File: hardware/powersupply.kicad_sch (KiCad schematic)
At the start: 34 parts, among them IC1 Battery_Charger, IC3 3.3V_Buck, J1 Battery, J1 Switch_In, J1 Switch_Out, J1 USB-C, Q2 PMV50XPAR, U2 5V_Boost

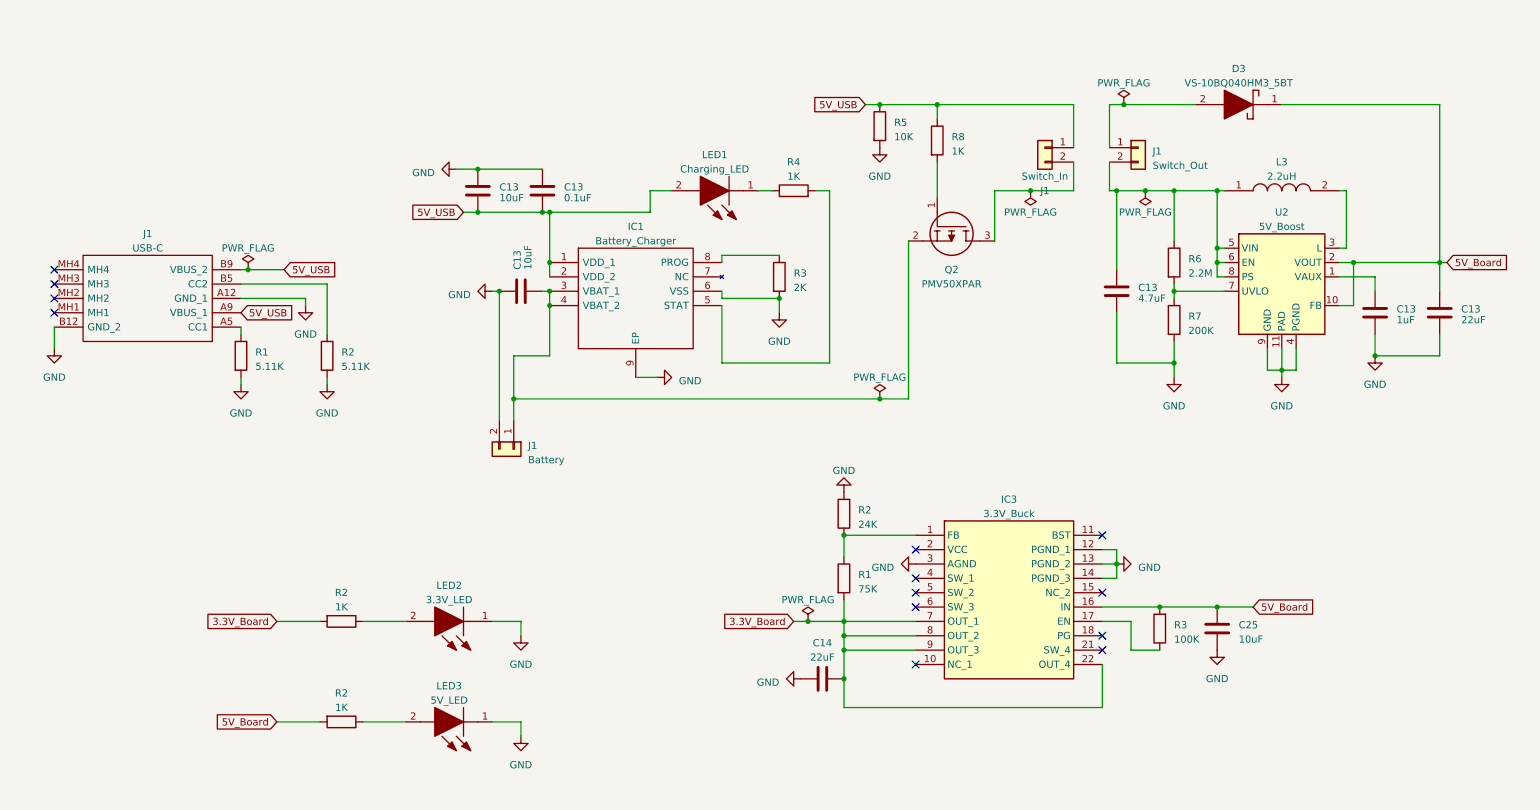
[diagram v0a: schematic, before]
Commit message: Change STM code to support an I2C bus. Add encoder reading code - tested on TIM1.
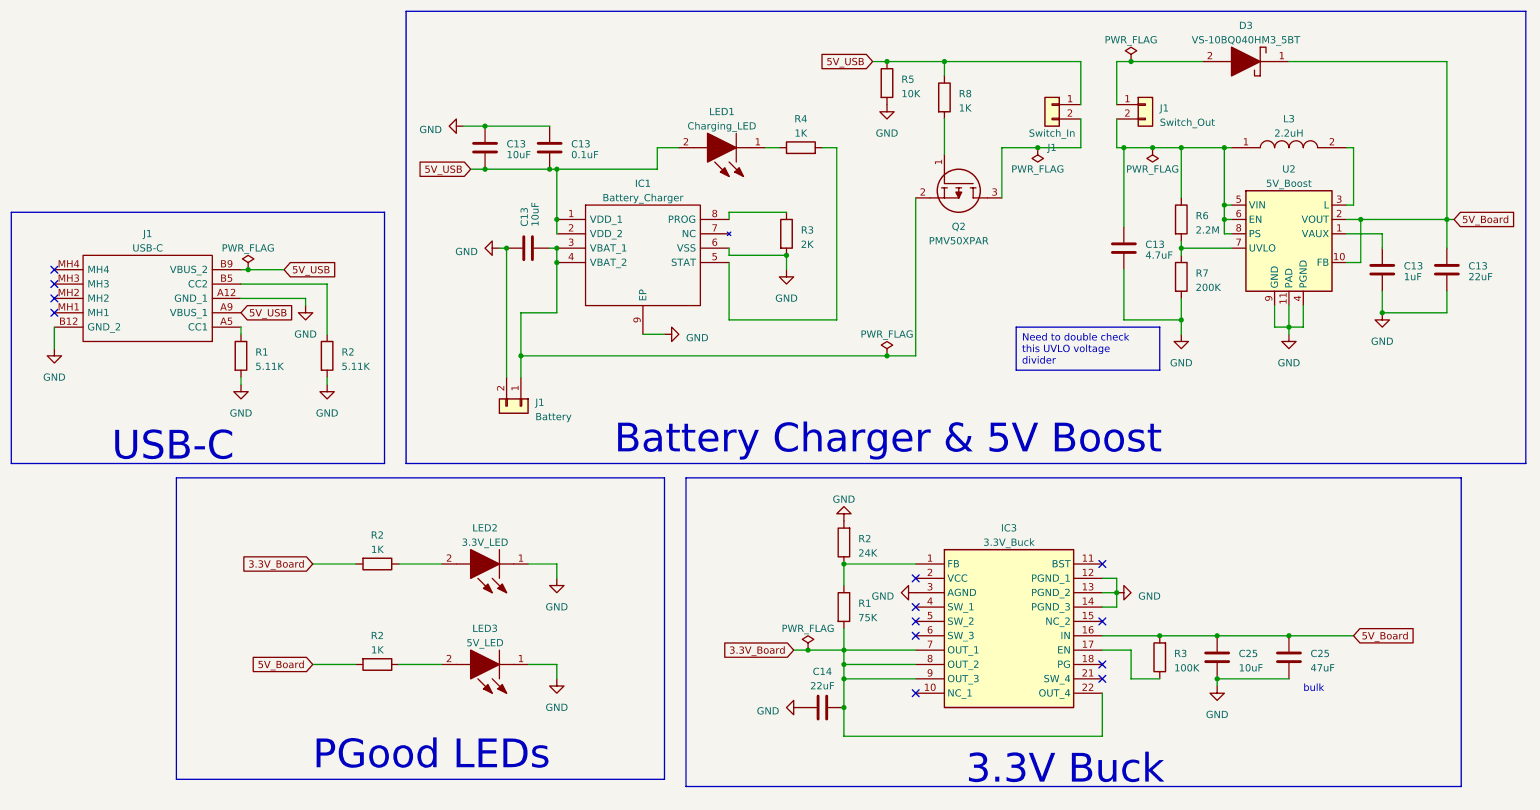
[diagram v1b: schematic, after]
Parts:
- added C25: 47uF, Capacitor_SMD:C_0805_2012Metric, symbol Device:C
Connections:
- net 5V_Board: now also C25.1
- net GND: now also C25.2
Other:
- note added: "3.3V Buck"
- note added: "Battery Charger & 5V Boost"
- note added: "PGood LEDs"
- note added: "USB-C"
- note added: "bulk"
- moved on the sheet: C13, C14, C25, D3, IC1, IC3, J1, L3, LED1, LED2, LED3, Q2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

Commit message: Add past project scripts. Add more lib components.
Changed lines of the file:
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@@
     (fill (type none))
+  )
+  (text_box "500mAh Battery:\nhttps://www.mouser.com/ProductDetail/406-ASR00035"
+    (at 114.3 91.44 0) (size 55.88 5.08)
+    (stroke (width 0) (type default))
+    (fill (type none))
+    (effects (font (size 1.27 1.27)) (justify left top))
   )
   (text_box "Need to double check this UVLO voltage divider"
